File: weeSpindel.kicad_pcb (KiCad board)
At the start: 2 copper layers, 46.5 x 20 mm, 21 parts, among them J1 POWER, J2 MPU-6050, U1 ESP-12E, U2 HT7733SA, U3 DS18B20

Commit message: another rev
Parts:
- moved U3 21.9 mm to (135.6, 111.8), turned to 180 degrees
- moved R3 15.3 mm to (131.8, 109.4), turned to 0 degrees
- moved C3 6.12 mm to (118.6, 111.9)
- moved C4 6.12 mm to (116.4, 111.9)
- moved C5 6.12 mm to (113.6, 111.1)
- moved U2 5.50 mm to (122.0, 110.5)
- moved L1 5.00 mm to (126.5, 110.3)
- moved C2 1.33 mm to (131.2, 104.6)
- moved J1 1.30 mm to (134.2, 103.4)
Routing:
- net GPIO12: track 19.6 -> 40.4 mm
- net 3V3: track 75.2 -> 71.1 mm
- net GND: track 3.17 -> 0.00 mm
- net VBAT: track 23.8 -> 25.3 mm
- net ADC: track 41.4 -> 42.3 mm
- net SCL: track 35.6 -> 36.3 mm
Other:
- board text added: "cperiod 2020 weeSpindel v1.0"
- board text removed: "v1.0"

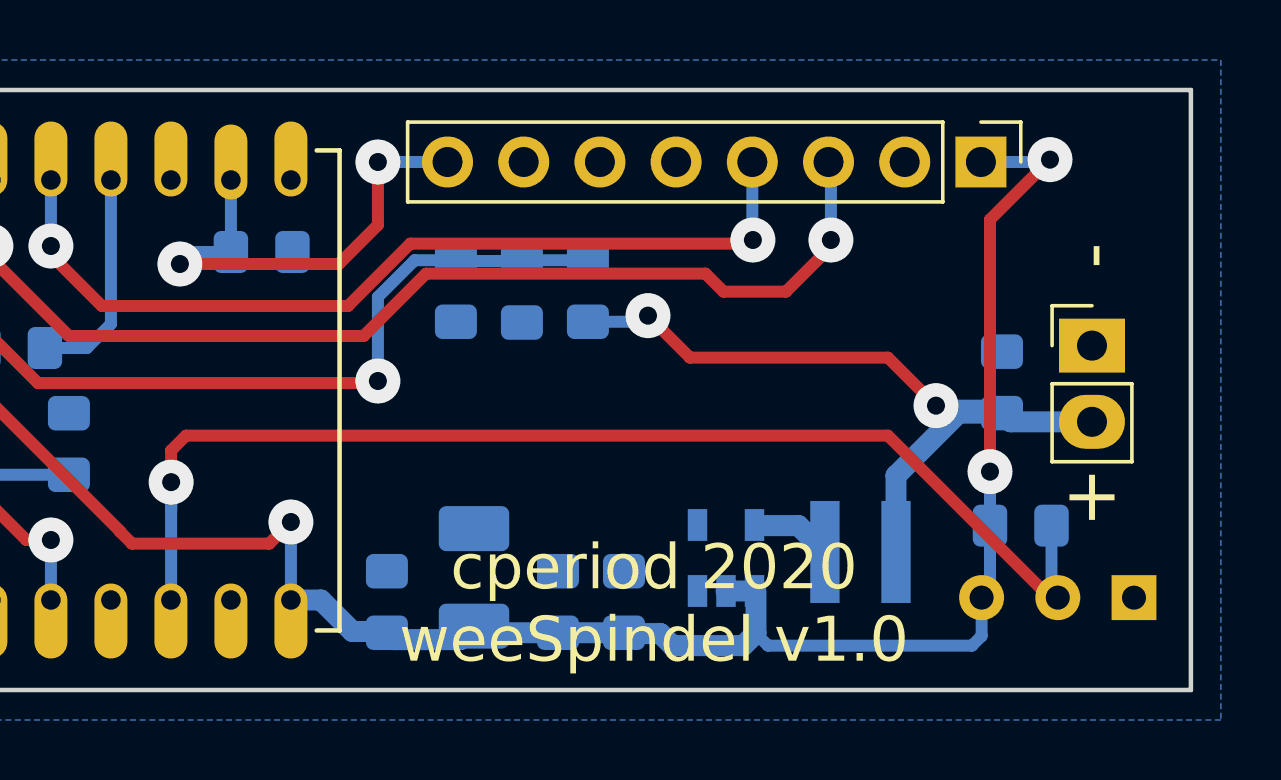
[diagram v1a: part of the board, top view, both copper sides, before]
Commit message: add a calibrate jumper
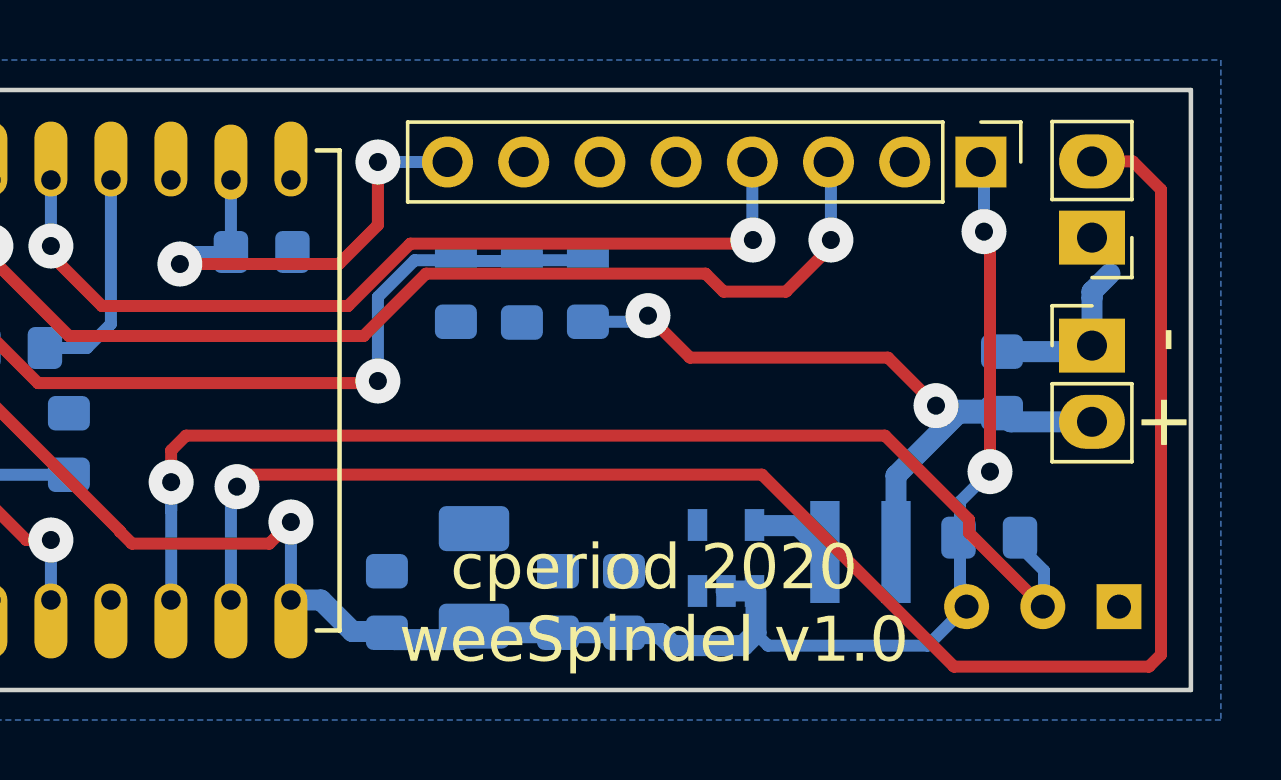
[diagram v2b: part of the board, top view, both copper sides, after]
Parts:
- added JP1: Cal, CPB:Socket_Strip_Straight_1x02_Oval_Pitch2.54mm, F.Cu at (134.2, 99.8)
- moved R3 1.12 mm to (130.8, 109.8)
- moved U3 0.58 mm to (135.1, 112.1)
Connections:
- net GPIO12 renamed DQ
- U1 pad 7: (no net) -> Net-(JP1-Pad2)
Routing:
- net Net-(JP1-Pad2): track 0.00 -> 55.8 mm, vias 0 -> 1
- net GND: track 0.00 -> 5.73 mm
- net 3V3: track 71.1 -> 67.3 mm

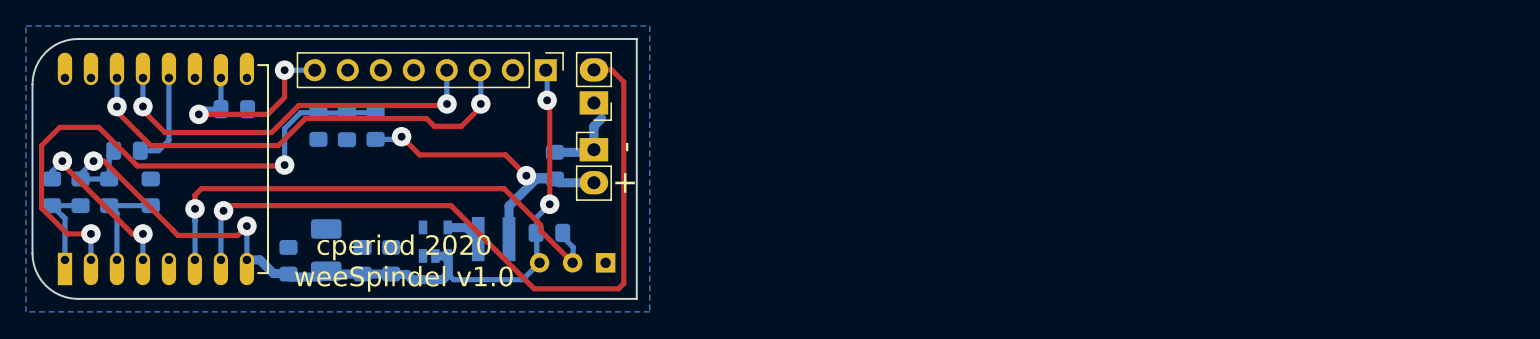
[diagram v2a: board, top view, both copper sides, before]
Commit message: now with integrated battery, power switch.
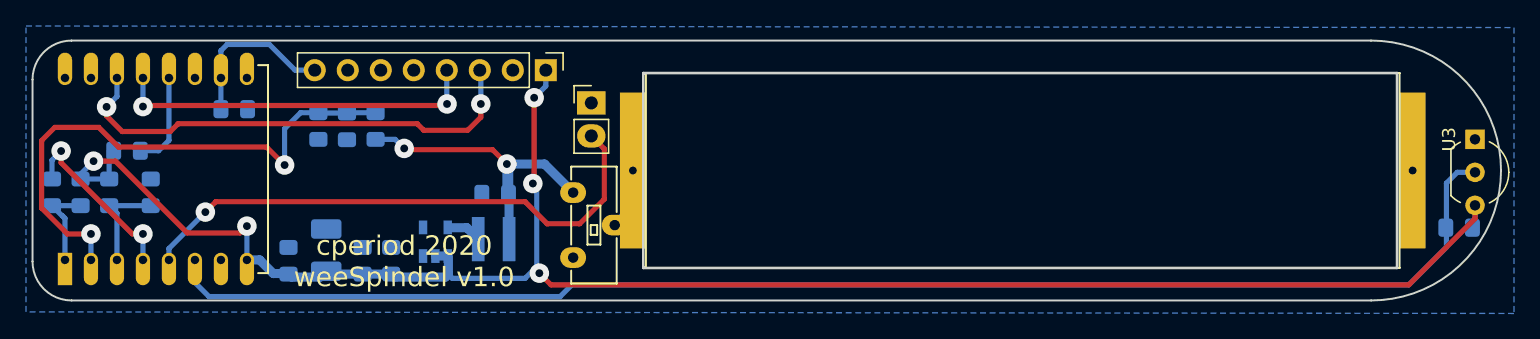
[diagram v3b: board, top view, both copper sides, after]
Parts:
- removed J1: POWER, CPB:Socket_Strip_Straight_1x02_Oval_Pitch2.54mm
- added BT1: AA, CPB:Battery_Springs_AA, F.Cu at (167.2, 105.0)
- added SW1: POWER, CPB:SPST Switch 9mmx3.5mm C223839, F.Cu at (134.2, 109.2)
- U3: moved to F.Cu
- moved R3 70.0 mm to (200.8, 109.4), turned to 180 degrees
- moved U3 67.6 mm to (202.0, 102.6), turned to 270 degrees
- moved C2 5.09 mm to (126.6, 106.8), turned to 180 degrees
- moved JP1 0.20 mm to (134.0, 99.8), turned to 0 degrees
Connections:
- U1 pad 5: (no net) -> Net-(JP1-Pad2)
- U1 pad 7: Net-(JP1-Pad2) -> (no net)
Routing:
- net 3V3: track 67.3 -> 144.6 mm, vias 4 -> 5
- net DQ: track 40.5 -> 107.5 mm, vias 1 -> 0
- net Net-(JP1-Pad2): track 55.8 -> 42.6 mm
- net GND: track 5.73 -> 0.00 mm
- net Net-(BT1-Pad1): track 0.00 -> 4.86 mm
- net GPIO15: track 15.8 -> 12.7 mm, vias 2 -> 0
- net SDA: track 30.1 -> 28.3 mm
- net GPIO16: track 12.4 -> 13.9 mm
- net SCL: track 36.3 -> 37.1 mm
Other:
- board size 46.5 x 20 mm -> 113 x 20 mm
- board text removed: "+"
- board text removed: "-"

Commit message: that's not something I can solder...
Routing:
- net Net-(JP1-Pad2): track 42.6 -> 42.4 mm, vias 1 -> 2
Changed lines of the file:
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@@
     (thickness 1.6)
     (drawings 12)
-    (tracks 149)
+    (tracks 151)
     (zones 0)
     (modules 23)
@@
   (segment (start 101.497 97.879) (end 101.497 102.679) (width 0.4) (layer B.Cu) (net 12) (status 10))
   (segment (start 101.497 102.679) (end 100.697 103.479) (width 0.4) (layer B.Cu) (net 12))
-  (segment (start 135 107.2) (end 135 103.34) (width 0.4) (layer F.Cu) (net 13))
-  (segment (start 135 103.34) (end 134 102.34) (width 0.4) (layer F.Cu) (net 13))
-  (segment (start 133.1 109.1) (end 135 107.2) (width 0.4) (layer F.Cu) (net 13))
-  (segment (start 130.6 109.1) (end 133.1 109.1) (width 0.4) (layer F.Cu) (net 13))
   (segment (start 104.3 108.2) (end 101.497 111.003) (width 0.4) (layer B.Cu) (net 13))
-  (segment (start 104.3 108.2) (end 105.1 107.4) (width 0.4) (layer F.Cu) (net 13))
   (via (at 104.3 108.2) (size 1.5) (drill 0.6) (layers F.Cu B.Cu) (net 13))
   (segment (start 101.497 111.003) (end 101.497 111.879) (width 0.4) (layer B.Cu) (net 13))
-  (segment (start 105.1 107.4) (end 128.9 107.4) (width 0.4) (layer F.Cu) (net 13))
-  (segment (start 128.9 107.4) (end 130.6 109.1) (width 0.4) (layer F.Cu) (net 13))
+  (via (at 134 104.1) (size 1.5) (drill 0.6) (layers F.Cu B.Cu) (net 13))
+  (segment (start 134 104.1) (end 134 102.34) (width 0.4) (layer B.Cu) (net 13))
+  (segment (start 134.7 104.8) (end 134.7 107.5) (width 0.4) (layer F.Cu) (net 13))
+  (segment (start 134 104.1) (end 134.7 104.8) (width 0.4) (layer F.Cu) (net 13))
+  (segment (start 105.1 107.4) (end 104.3 108.2) (width 0.4) (layer F.Cu) (net 13))
+  (segment (start 134.7 107.5) (end 133.1 109.1) (width 0.4) (layer F.Cu) (net 13))
+  (segment (start 133.1 109.1) (end 130 109.1) (width 0.4) (layer F.Cu) (net 13))
+  (segment (start 130 109.1) (end 128.3 107.4) (width 0.4) (layer F.Cu) (net 13))
+  (segment (start 128.3 107.4) (end 105.1 107.4) (width 0.4) (layer F.Cu) (net 13))
   (segment (start 200.635 105.14) (end 202 105.14) (width 0.4) (layer B.Cu) (net 14))
   (segment (start 199.8 110.9) (end 199.8 105.975) (width 0.4) (layer B.Cu) (net 14))
